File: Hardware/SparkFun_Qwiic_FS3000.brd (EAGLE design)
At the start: 85.1 x 103.6 mm, 327 parts, among them J11 QWIIC_RA, J12 QWIIC_RA, J15 QWIIC_RA, J18 QWIIC_RA, J19 QWIIC_RA, J2 QWIIC_RA, J3 QWIIC_RA, J4 QWIIC_RA, J8 QWIIC_RA, U1 FS3000, U2 FS3000, U3 FS3000, U4 FS3000, U5 FS3000, U6 FS3000

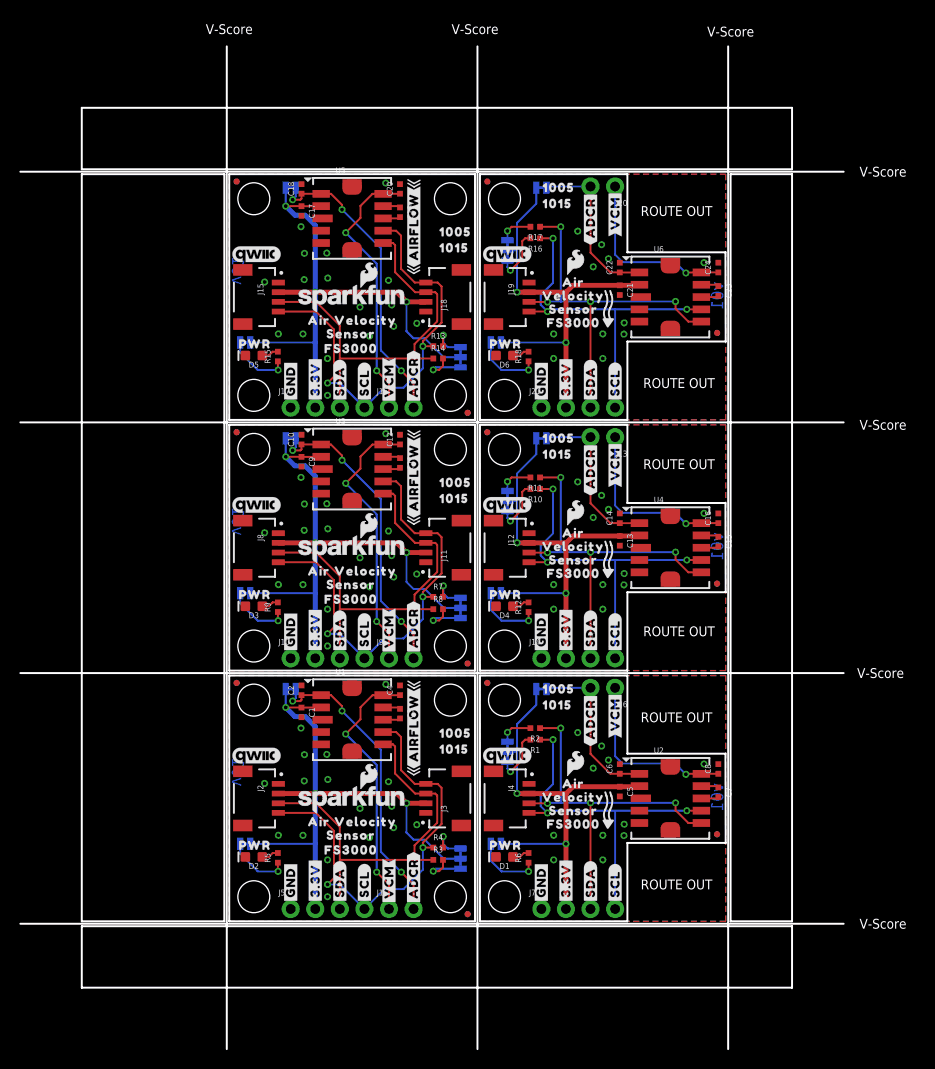
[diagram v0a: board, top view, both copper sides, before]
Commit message: Decided to use 1X1 version, bumped version to "v10"
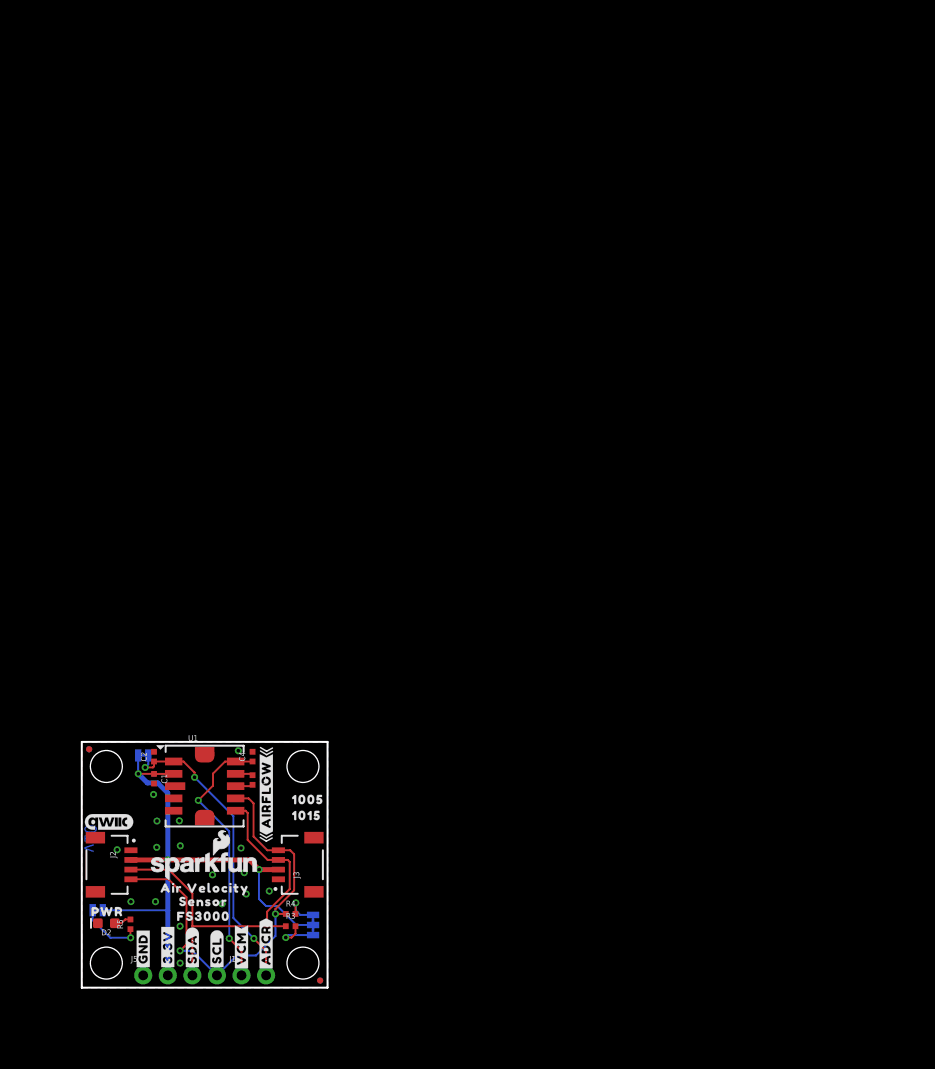
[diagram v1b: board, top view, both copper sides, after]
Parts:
- removed ADC-REF1, ADC-REF2, ADC-REF3, ADC-REF4, ADC-REF5: (no value), SparkFun-Jumpers:SMT-JUMPER_2_NC_TRACE_SILK
- removed C10, C11, C13, C14, C15, C17, C18, C19, C21, C22, C23, C5, C6, C7, C9: 0.1uF, SparkFun-Capacitors:0402-TIGHT
- removed C12, C16, C20, C24, C8: 1.0uF, SparkFun-Capacitors:0402-TIGHT
- removed D1, D3, D4, D5, D6: RED, SparkFun-LED:LED-0603
- removed I2C1, I2C2, I2C3, I2C4, I2C5: (no value), SparkFun-Jumpers:SMT-JUMPER_3_2-NC_TRACE_SILK
- removed J10, J14, J17, J21, J7: (no value), SparkFun-Connectors:1X04_NO_SILK
- removed J11, J12, J15, J18, J19, J4, J8: QWIIC_RA, SparkFun-Connectors:JST04_1MM_RA
- removed J13, J16, J20, J6, J9: (no value), SparkFun-Connectors:1X02_NO_SILK
- removed JP10, JP12, JP13, JP14, JP18, JP19, JP20, JP21, JP27, JP28, JP29, JP30, JP34, JP35, JP36, JP37, JP43, JP44, JP45, JP46: FIDUCIALUFIDUCIAL, SparkFun-Aesthetics:FIDUCIAL-MICRO
- removed JP15, JP17, JP22, JP24, JP25, JP26, JP31, JP33, JP38, JP40, JP41, JP42, JP47, JP9: STAND-OFF, SparkFun-Hardware:STAND-OFF
- removed JP16, JP23, JP32, JP39, JP48: LED, SparkFun-Jumpers:SMT-JUMPER_2_NC_TRACE_SILK
- removed LOGO10, LOGO14, LOGO18, LOGO22, LOGO6: QWIIC_LOGO_5MM, SparkFun-Aesthetics:QWIIC_5MM
- removed LOGO11, LOGO12, LOGO16, LOGO19, LOGO20, LOGO24, LOGO8: SFE_LOGO_NAME_FLAME.1_INCH, SparkFun-Aesthetics:SFE_LOGO_NAME_FLAME_.1
- removed LOGO13, LOGO17, LOGO2, LOGO21, LOGO9: OSHW-LOGOMINI, SparkFun-Aesthetics:OSHW-LOGO-MINI
- removed LOGO15, LOGO23, LOGO7: SFE_LOGO_FLAME.1_INCH, SparkFun-Aesthetics:SFE_LOGO_FLAME_.1
- removed R1, R10, R11, R13, R14, R16, R17, R2, R7, R8: 2.2k, SparkFun-Resistors:0402-TIGHT
- removed R12, R15, R18, R6, R9: 1k, SparkFun-Resistors:0402-TIGHT
- removed U$1, U$113, U$114, U$142, U$143, U$2, U$57, U$58, U$86, U$87: (no value), output:#GND#0
- removed U$100, U$152, U$156, U$40, U$44, U$96: (no value), output:#ADCR#0
- removed U$101, U$106, U$124, U$129, U$157, U$162, U$45, U$50, U$68, U$73: (no value), output:FS30001
- removed U$102, U$107, U$125, U$130, U$158, U$163, U$46, U$51, U$69, U$74: (no value), output:VELOCITY30003
- removed U$103, U$108, U$126, U$131, U$159, U$164, U$47, U$52, U$70, U$75: (no value), output:AIR30004
- removed U$104, U$109, U$127, U$132, U$160, U$165, U$48, U$53, U$71, U$76: (no value), output:SENSOR30005
- removed U$105, U$128, U$161, U$49, U$72: (no value), output:#ADC#REF#0
- removed U$110, U$136, U$166, U$54, U$80: (no value), output:10050
- removed U$111, U$137, U$167, U$55, U$81: (no value), output:10150
- removed U$112, U$168, U$56: (no value), output:I2C_ADR#_0X280
- removed U$115, U$116, U$144, U$145, U$32, U$33, U$59, U$60, U$88, U$89: (no value), output:#3#3V#0
- removed U$117, U$123, U$146, U$154, U$34, U$42, U$61, U$67, U$90, U$98: (no value), output:#SDA#0
- removed U$118, U$122, U$147, U$153, U$35, U$41, U$62, U$66, U$91, U$97: (no value), output:#SCL#0
- removed U$119, U$148, U$36, U$63, U$92: (no value), output:#LED#0
- removed U$120, U$149, U$37, U$64, U$93: (no value), output:PWR0
- removed U$121, U$150, U$38, U$65, U$94: (no value), output:#I2C#0
- removed U$133, U$134, U$77, U$78: (no value), output:#AIRFLOW#0
- removed U$135, U$79: (no value), output:I2C_ADD#_0X280
- removed U$138, U$139, U$82, U$83: (no value), FS3000:#ADCR#4
- removed U$140, U$141, U$84, U$85: (no value), FS3000:#VCM#3
- removed U$151, U$155, U$39, U$43, U$95, U$99: (no value), output:#VCM#0
- removed U2, U3, U4, U5, U6: FS3000, FS3000:FS3000
- added FRAME1: FRAME-LETTER, SparkFun-Aesthetics:CREATIVE_COMMONS
- moved U$28 16.7 mm to (19.2, 13.7)
- moved ADC-REF 16.7 mm to (6.35, 24.0)
- moved C1 16.7 mm to (7.47, 21.6)
- moved C2 16.7 mm to (7.47, 23.9)
- moved C3 16.7 mm to (17.7, 21.5)
- moved C4 16.7 mm to (17.7, 23.9)
- moved D2 16.7 mm to (2.54, 6.65)
- moved I2C 16.7 mm to (23.9, 6.48)
- moved J1 16.7 mm to (16.5, 1.27)
- moved J2 16.7 mm to (5.08, 12.7)
- moved J3 16.7 mm to (20.3, 12.7)
- moved J5 16.7 mm to (6.35, 1.27)
- moved JP1 16.7 mm to (1.65, 8.00)
- moved JP11 16.7 mm to (24.6, 0.74)
- moved JP2 16.7 mm to (24.6, 0.74)
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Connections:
- removed net 3.3V1: ADC-REF1.1, C5.1, I2C1.2, J4.2, J7.2, JP16.2, U2.2
- removed net 3.3V2: ADC-REF2.1, C9.1, I2C2.2, J10.2, J11.2, J8.2, JP23.2, U3.2
- removed net 3.3V3: ADC-REF3.1, C13.1, I2C3.2, J12.2, J14.2, JP32.2, U4.2
- removed net 3.3V4: ADC-REF4.1, C17.1, I2C4.2, J15.2, J17.2, J18.2, JP39.2, U5.2
- removed net 3.3V5: ADC-REF5.1, C21.1, I2C5.2, J19.2, J21.2, JP48.2, U6.2
- removed net ADC-REF1: ADC-REF1.2, C6.1, J6.2, U2.1
- removed net ADC-REF2: ADC-REF2.2, C10.1, J9.2, U3.1
- removed net ADC-REF3: ADC-REF3.2, C14.1, J13.2, U4.1
- removed net ADC-REF4: ADC-REF4.2, C18.1, J16.2, U5.1
- removed net ADC-REF5: ADC-REF5.2, C22.1, J20.2, U6.1
- removed net GND1: C5.2, C6.2, C8.2, D1.C, J4.1, J7.1, U2.3
- removed net GND2: C10.2, C12.2, C9.2, D3.C, J10.1, J11.1, J8.1, U3.3
- removed net GND3: C13.2, C14.2, C16.2, D4.C, J12.1, J14.1, U4.3
- removed net GND4: C17.2, C18.2, C20.2, D5.C, J15.1, J17.1, J18.1, U5.3
- removed net GND5: C21.2, C22.2, C24.2, D6.C, J19.1, J21.1, U6.3
- removed net N$10: JP16.1, R6.1
- removed net N$11: C7.1, U2.9
- removed net N$12: C7.2, U2.8
- removed net N$13: I2C2.1, R8.2
- removed net N$14: I2C2.3, R7.2
- removed net N$15: D3.A, R9.2
- removed net N$16: JP23.1, R9.1
- removed net N$17: C11.1, U3.9
- removed net N$18: C11.2, U3.8
- removed net N$19: I2C3.1, R11.2
- removed net N$20: I2C3.3, R10.2
- removed net N$21: D4.A, R12.2
- removed net N$22: JP32.1, R12.1
- removed net N$23: C15.1, U4.9
- removed net N$24: C15.2, U4.8
- removed net N$25: I2C4.1, R14.2
- removed net N$26: I2C4.3, R13.2
- removed net N$27: D5.A, R15.2
- removed net N$28: JP39.1, R15.1
- removed net N$29: C19.1, U5.9
- removed net N$30: C19.2, U5.8
- removed net N$31: I2C5.1, R17.2
- removed net N$32: I2C5.3, R16.2
- removed net N$33: D6.A, R18.2
- removed net N$34: JP48.1, R18.1
- removed net N$35: C23.1, U6.9
- removed net N$36: C23.2, U6.8
- removed net N$5: I2C1.1, R2.2
- removed net N$7: I2C1.3, R1.2
- removed net N$9: D1.A, R6.2
- removed net SCL1: J4.4, J7.4, R1.1, U2.7
- removed net SCL2: J10.4, J11.4, J8.4, R7.1, U3.7
- removed net SCL3: J12.4, J14.4, R10.1, U4.7
- removed net SCL4: J15.4, J17.4, J18.4, R13.1, U5.7
- removed net SCL5: J19.4, J21.4, R16.1, U6.7
- removed net SDA1: J4.3, J7.3, R2.1, U2.6
- removed net SDA2: J10.3, J11.3, J8.3, R8.1, U3.6
- removed net SDA3: J12.3, J14.3, R11.1, U4.6
- removed net SDA4: J15.3, J17.3, J18.3, R14.1, U5.6
- removed net SDA5: J19.3, J21.3, R17.1, U6.6
- removed net VCM1: C8.1, J6.1, U2.10
- removed net VCM2: C12.1, J9.1, U3.10
- removed net VCM3: C16.1, J13.1, U4.10
- removed net VCM4: C20.1, J16.1, U5.10
- removed net VCM5: C24.1, J20.1, U6.10
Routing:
- net 3.3V4: track 60.4 -> 0.00 mm, vias 3 -> 0
- net 3.3V2: track 60.4 -> 0.00 mm, vias 3 -> 0
- net SCL2: track 45.7 -> 0.00 mm, vias 2 -> 0
- net SCL4: track 45.7 -> 0.00 mm, vias 2 -> 0
- net 3.3V5: track 44.2 -> 0.00 mm, vias 2 -> 0
- net 3.3V3: track 44.2 -> 0.00 mm, vias 2 -> 0
- net 3.3V1: track 44.2 -> 0.00 mm, vias 2 -> 0
- net SDA2: track 42.5 -> 0.00 mm
- net SDA4: track 42.5 -> 0.00 mm
- net SDA3: track 40.0 -> 0.00 mm, vias 4 -> 0
- net SDA5: track 40.0 -> 0.00 mm, vias 4 -> 0
- net SDA1: track 40.0 -> 0.00 mm, vias 4 -> 0
- net SCL5: track 37.8 -> 0.00 mm, vias 3 -> 0
- net SCL3: track 37.8 -> 0.00 mm, vias 3 -> 0
- net SCL1: track 37.8 -> 0.00 mm, vias 3 -> 0
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- removed copper zone on layer 1, net GND1
- removed copper zone on layer 16, net GND1
- removed copper zone on layer 1, net GND2
- removed copper zone on layer 16, net GND2
- removed copper zone on layer 1, net GND3
- removed copper zone on layer 16, net GND3
- removed copper zone on layer 1, net GND4
- removed copper zone on layer 16, net GND4
- removed copper zone on layer 1, net GND5
- removed copper zone on layer 16, net GND5
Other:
- board size 85.1 x 103.6 mm -> 25.4 x 25.4 mm
- board text added: "Measure Units: INCHES"
- board text added: "Pete Lewis"
- board text added: "v10"
- board text removed: "ROUTE OUT"
- board text removed: "V-Score"
- board text removed: "v01"
